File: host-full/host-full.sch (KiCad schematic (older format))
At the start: 17 parts, among them J1 CONN_INTEGRALSTICK_MCU_HOST, J15 XILINX_JTAG, J16 Conn_Coaxial, J17 Conn_Coaxial, J18 Conn_Coaxial, J19 Conn_Coaxial, J2 CONN_INTEGRALSTICK_FPGA_HOST, J20 Conn_Coaxial, J21 Conn_Coaxial, SW1 SW_SPST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

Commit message: Finished initial schematic review
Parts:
- added J23: PMOD_HOST, symbol special-azonenberg:PMOD_HOST
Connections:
- net 3V3: now also J23.12 (3V3), J23.6 (3V3)
- net GND: now also J23.11 (GND), J23.5 (GND)
- net LVDS_DQ5_N: now reaches J2.21 (LVDS_DQ5_N)
- net LVDS_DQ5_N: now also J23.10 (D7)
- net LVDS_DQ4_N: now reaches J2.22 (LVDS_DQ4_N)
- net LVDS_DQ4_N: now also J23.8 (D5)
- net LVDS_DQ5_P: now reaches J2.23 (LVDS_DQ5_P)
- net LVDS_DQ5_P: now also J23.9 (D6)
- net LVDS_DQ4_P: now reaches J2.24 (LVDS_DQ4_P)
- net LVDS_DQ4_P: now also J23.7 (D4)
- net LVDS_DQ3_N: now reaches J2.27 (LVDS_DQ3_N)
- net LVDS_DQ3_N: now also J23.4 (D3)
- net LVDS_DQ2_N: now reaches J2.28 (LVDS_DQ2_N)
- net LVDS_DQ2_N: now also J23.2 (D1)
- net LVDS_DQ3_P: now reaches J2.29 (LVDS_DQ3_P)
- net LVDS_DQ3_P: now also J23.3 (D2)
- net LVDS_DQ2_P: now reaches J2.30 (LVDS_DQ2_P)
- net LVDS_DQ2_P: now also J23.1 (D0)
- no-connect marks 16 -> 8
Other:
- note removed: "Ethernet 2V5, 1V2 are high power rails we need to generate\n1V8, 3V3 are just RGMII power"
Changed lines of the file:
@@
 Sheet 1 4
 Title "INTEGRALSTICK Full Host"
-Date "2019-11-03"
+Date "2019-11-04"
 Rev "0.1"
 Comp "Antikernel Labs"
@@
 Comment4 ""
 $EndDescr
-$Comp
-L special-azonenberg:CONN_INTEGRALSTICK_FPGA_HOST J2
-U 3 1 5DBBCD32
-P 9600 5900
-F 0 "J2" H 9600 5850 50  0000 L CNN
-F 1 "CONN_INTEGRALSTICK_FPGA_HOST" H 9600 5750 50  0000 L CNN
-F 2 "" H 9600 5900 50  0001 C CNN
-F 3 "" H 9600 5900 50  0001 C CNN
-	3    9600 5900
-	1    0    0    -1
-$EndComp
 $Sheet
 S 700  850  800  650
@@
 F1 "psu.sch" 50
 F2 "GND" O R 1500 1400 50
-F4 "3V3" O R 1500 1000 50
-F5 "1V8" O R 1500 1200 50
+F3 "3V3" O R 1500 1000 50
+F4 "1V8" O R 1500 1200 50
+F5 "2V5" O R 1500 1100 50
+F6 "1V2" O R 1500 1300 50
 $EndSheet
 $Sheet
@@
 Text Label 1800 5750 0    50   ~ 0
 3V3
-Text Notes 700  700  0    50   ~ 0
-Ethernet 2V5, 1V2 are high power rails we need to generate\n1V8, 3V3 are just RGMII power
 Text Label 1500 2450 0    50   ~ 0
-ETH_2V5
+2V5
 Text Label 1500 2350 0    50   ~ 0
 3V3
@@
 1V8
 Text Label 1500 2650 0    50   ~ 0
-ETH_1V2
+1V2
 Text Label 1800 5850 0    50   ~ 0
 GND
@@
 Text Label 9400 3450 2    50   ~ 0
 LVDS_DQ1_N
-NoConn ~ 9400 3650
-NoConn ~ 9400 3750
-NoConn ~ 9400 3950
-NoConn ~ 9400 4050
-NoConn ~ 9400 4250
-NoConn ~ 9400 4350
-NoConn ~ 9400 4550
-NoConn ~ 9400 4650
 NoConn ~ 9400 4850
 NoConn ~ 9400 4950
@@
 Text Label 9400 5850 2    50   ~ 0
 ETH0_LED2_P
+Text Label 1500 1100 0    50   ~ 0
+2V5
+Text Label 1500 1300 0    50   ~ 0
+1V2
+Wire Wire Line
+	7000 3200 7000 3300
+Wire Wire Line
+	7000 3400 7000 3500
+Text Label 7000 3700 0    50   ~ 0
+LVDS_DQ2_P
+Text Label 7000 3800 0    50   ~ 0
+LVDS_DQ2_N
+Text Label 7000 3900 0    50   ~ 0
+LVDS_DQ3_P
+Text Label 7000 4000 0    50   ~ 0
+LVDS_DQ3_N
+Text Label 7000 4100 0    50   ~ 0
+LVDS_DQ4_P
+Text Label 7000 4200 0    50   ~ 0
+LVDS_DQ4_N
+$Comp
+L special-azonenberg:PMOD_HOST J?
+U 1 1 5E1F1FA5
+P 6800 4450
+AR Path="/5DF8FFFE/5E1F1FA5" Ref="J?"  Part="1"
+AR Path="/5E1F1FA5" Ref="J23"  Part="1"
+F 0 "J23" H 6867 5947 60  0000 C CNN
+F 1 "PMOD_HOST" H 6867 5841 60  0000 C CNN
+F 2 "" H 6800 4450 60  0001 C CNN
+F 3 "" H 6800 4450 60  0001 C CNN
+	1    6800 4450
+	-1   0    0    -1
+$EndComp
+Text Label 7000 4300 0    50   ~ 0
+LVDS_DQ5_P
+Text Label 7000 4400 0    50   ~ 0
+LVDS_DQ5_N
+$Comp
+L special-azonenberg:CONN_INTEGRALSTICK_FPGA_HOST J2
+U 3 1 5DBBCD32
+P 9600 5900
+F 0 "J2" H 9600 5850 50  0000 L CNN
+F 1 "CONN_INTEGRALSTICK_FPGA_HOST" H 9600 5750 50  0000 L CNN
+F 2 "" H 9600 5900 50  0001 C CNN
+F 3 "" H 9600 5900 50  0001 C CNN
+	3    9600 5900
+	1    0    0    -1
+$EndComp
+Text Label 9400 3650 2    50   ~ 0
+LVDS_DQ2_P
+Text Label 9400 3750 2    50   ~ 0
+LVDS_DQ2_N
+Text Label 9400 3950 2    50   ~ 0
+LVDS_DQ3_P
+Text Label 9400 4050 2    50   ~ 0
+LVDS_DQ3_N
+Text Label 9400 4250 2    50   ~ 0
+LVDS_DQ4_P
+Text Label 9400 4350 2    50   ~ 0
+LVDS_DQ4_N
+Text Label 9400 4550 2    50   ~ 0
+LVDS_DQ5_P
+Text Label 9400 4650 2    50   ~ 0
+LVDS_DQ5_N
+Text Label 7000 3200 0    50   ~ 0
+3V3
+Text Label 7000 3400 0    50   ~ 0
+GND
 $EndSCHEMATC

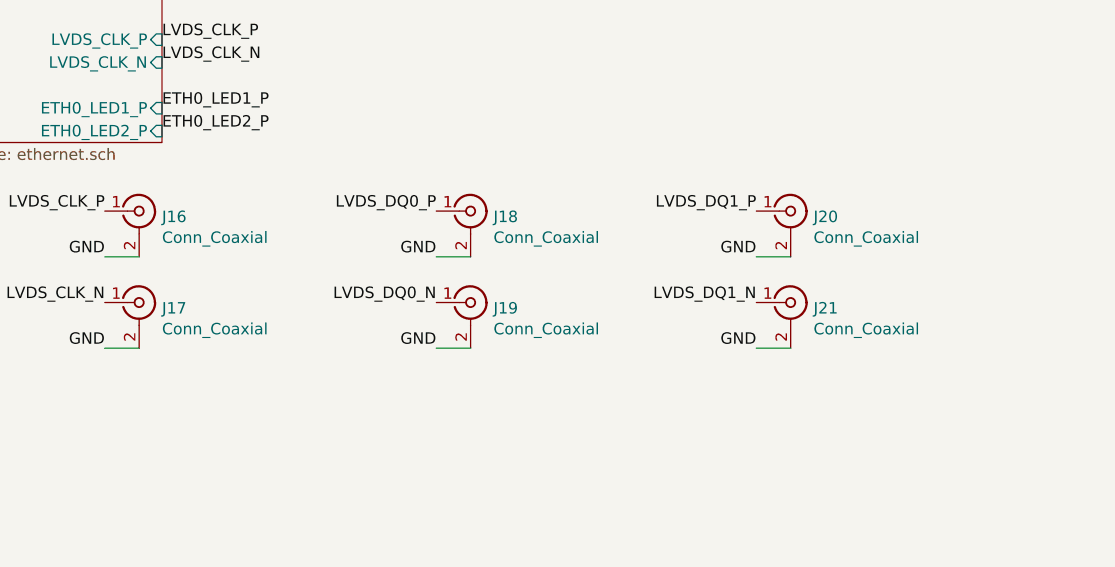
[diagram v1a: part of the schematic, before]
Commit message: Initial layout on host-full. Rough floorplan is finalized, all MCU PMODs routed.
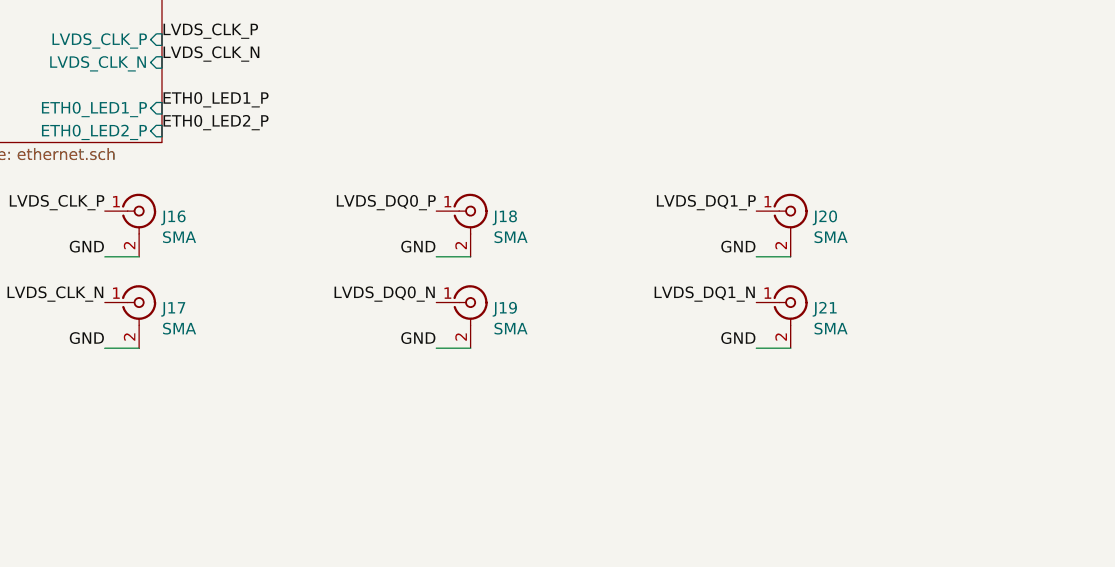
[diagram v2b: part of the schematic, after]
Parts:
- D1: footprint (none) -> azonenberg_pcb:EIA_0603_LED
- J1, J2: footprint (none) -> azonenberg_pcb:CONN_SAMTEC_QSH-060-01-L-D-A
- J15: footprint (none) -> azonenberg_pcb:XILINX_JTAG_PTH_MOLEX_0878311420
- J16, J17, J18, J19, J20, J21: value Conn_Coaxial -> SMA; footprint (none) -> azonenberg_pcb:CONN_SMA_EDGE_SAMTEC_SMA_J_P_H_ST_EM1
- J23: footprint (none) -> azonenberg_pcb:CONN_HEADER_2.54MM_2x6_RA_PMOD_HOST
- R49, R50, R51, R52: footprint (none) -> azonenberg_pcb:EIA_0402_RES_NOSILK
- SW1, SW2, SW3: footprint (none) -> azonenberg_pcb:SWITCH_RAFI_MICON_5
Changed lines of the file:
@@
 Sheet 1 4
 Title "INTEGRALSTICK Full Host"
-Date "2019-11-04"
+Date "2019-11-07"
 Rev "0.1"
 Comp "Antikernel Labs"
@@
 F 0 "J1" H 3578 6901 50  0000 L CNN
 F 1 "CONN_INTEGRALSTICK_MCU_HOST" H 3578 6810 50  0000 L CNN
-F 2 "" H 3000 6400 50  0001 C CNN
+F 2 "azonenberg_pcb:CONN_SAMTEC_QSH-060-01-L-D-A" H 3000 6400 50  0001 C CNN
 F 3 "" H 3000 6400 50  0001 C CNN
 	2    3000 6400
@@
 F 0 "SW1" V 3004 6998 50  0000 L CNN
 F 1 "SW_SPST" V 3095 6998 50  0000 L CNN
-F 2 "" H 3050 6900 50  0001 C CNN
+F 2 "azonenberg_pcb:SWITCH_RAFI_MICON_5" H 3050 6900 50  0001 C CNN
 F 3 "" H 3050 6900 50  0001 C CNN
 	1    3050 6900
@@
 F 0 "J15" H 2138 8397 60  0000 C CNN
 F 1 "XILINX_JTAG" H 2138 8291 60  0000 C CNN
-F 2 "" H 1800 6850 60  0000 C CNN
+F 2 "azonenberg_pcb:XILINX_JTAG_PTH_MOLEX_0878311420" H 1800 6850 60  0001 C CNN
 F 3 "" H 1800 6850 60  0000 C CNN
 	1    1800 6850
@@
 F 0 "R49" H 3120 7296 50  0000 L CNN
 F 1 "DNP" H 3120 7205 50  0000 L CNN
-F 2 "" V 2980 7250 50  0001 C CNN
+F 2 "azonenberg_pcb:EIA_0402_RES_NOSILK" V 2980 7250 50  0001 C CNN
 F 3 "" H 3050 7250 50  0001 C CNN
 	1    3050 7250
@@
 F 0 "R50" H 4020 6996 50  0000 L CNN
 F 1 "DNP" H 4020 6905 50  0000 L CNN
-F 2 "" V 3880 6950 50  0001 C CNN
+F 2 "azonenberg_pcb:EIA_0402_RES_NOSILK" V 3880 6950 50  0001 C CNN
 F 3 "" H 3950 6950 50  0001 C CNN
 	1    3950 6950
@@
 F 0 "SW2" V 3904 7398 50  0000 L CNN
 F 1 "SW_SPST" V 3995 7398 50  0000 L CNN
-F 2 "" H 3950 7300 50  0001 C CNN
+F 2 "azonenberg_pcb:SWITCH_RAFI_MICON_5" H 3950 7300 50  0001 C CNN
 F 3 "" H 3950 7300 50  0001 C CNN
 	1    3950 7300
@@
 F 0 "R51" H 4920 6996 50  0000 L CNN
 F 1 "DNP" H 4920 6905 50  0000 L CNN
-F 2 "" V 4780 6950 50  0001 C CNN
+F 2 "azonenberg_pcb:EIA_0402_RES_NOSILK" V 4780 6950 50  0001 C CNN
 F 3 "" H 4850 6950 50  0001 C CNN
 	1    4850 6950
@@
 F 0 "SW3" V 4804 7398 50  0000 L CNN
 F 1 "SW_SPST" V 4895 7398 50  0000 L CNN
-F 2 "" H 4850 7300 50  0001 C CNN
+F 2 "azonenberg_pcb:SWITCH_RAFI_MICON_5" H 4850 7300 50  0001 C CNN
 F 3 "" H 4850 7300 50  0001 C CNN
 	1    4850 7300
@@
 F 0 "R52" H 5770 6996 50  0000 L CNN
 F 1 "270" H 5770 6905 50  0000 L CNN
-F 2 "" V 5630 6950 50  0001 C CNN
+F 2 "azonenberg_pcb:EIA_0402_RES_NOSILK" V 5630 6950 50  0001 C CNN
 F 3 "" H 5700 6950 50  0001 C CNN
 	1    5700 6950
@@
 F 0 "D1" V 5739 7132 50  0000 R CNN
 F 1 "GREEN" V 5648 7132 50  0000 R CNN
-F 2 "" H 5700 7250 50  0001 C CNN
+F 2 "azonenberg_pcb:EIA_0603_LED" H 5700 7250 50  0001 C CNN
 F 3 "~" H 5700 7250 50  0001 C CNN
 	1    5700 7250
@@
 P 1400 3700
 F 0 "J16" H 1500 3675 50  0000 L CNN
-F 1 "Conn_Coaxial" H 1500 3584 50  0000 L CNN
-F 2 "" H 1400 3700 50  0001 C CNN
+F 1 "SMA" H 1500 3584 50  0000 L CNN
+F 2 "azonenberg_pcb:CONN_SMA_EDGE_SAMTEC_SMA_J_P_H_ST_EM1" H 1400 3700 50  0001 C CNN
 F 3 "" H 1400 3700 50  0001 C CNN
 	1    1400 3700
@@
 P 1400 4100
 F 0 "J17" H 1500 4075 50  0000 L CNN
-F 1 "Conn_Coaxial" H 1500 3984 50  0000 L CNN
-F 2 "" H 1400 4100 50  0001 C CNN
+F 1 "SMA" H 1500 3984 50  0000 L CNN
+F 2 "azonenberg_pcb:CONN_SMA_EDGE_SAMTEC_SMA_J_P_H_ST_EM1" H 1400 4100 50  0001 C CNN
 F 3 "" H 1400 4100 50  0001 C CNN
 	1    1400 4100
@@
 P 2850 3700
 F 0 "J18" H 2950 3675 50  0000 L CNN
-F 1 "Conn_Coaxial" H 2950 3584 50  0000 L CNN
-F 2 "" H 2850 3700 50  0001 C CNN
+F 1 "SMA" H 2950 3584 50  0000 L CNN
+F 2 "azonenberg_pcb:CONN_SMA_EDGE_SAMTEC_SMA_J_P_H_ST_EM1" H 2850 3700 50  0001 C CNN
 F 3 "" H 2850 3700 50  0001 C CNN
 	1    2850 3700
@@
 P 2850 4100
 F 0 "J19" H 2950 4075 50  0000 L CNN
-F 1 "Conn_Coaxial" H 2950 3984 50  0000 L CNN
-F 2 "" H 2850 4100 50  0001 C CNN
+F 1 "SMA" H 2950 3984 50  0000 L CNN
+F 2 "azonenberg_pcb:CONN_SMA_EDGE_SAMTEC_SMA_J_P_H_ST_EM1" H 2850 4100 50  0001 C CNN
 F 3 "" H 2850 4100 50  0001 C CNN
 	1    2850 4100
@@
 P 4250 3700
 F 0 "J20" H 4350 3675 50  0000 L CNN
-F 1 "Conn_Coaxial" H 4350 3584 50  0000 L CNN
-F 2 "" H 4250 3700 50  0001 C CNN
+F 1 "SMA" H 4350 3584 50  0000 L CNN
+F 2 "azonenberg_pcb:CONN_SMA_EDGE_SAMTEC_SMA_J_P_H_ST_EM1" H 4250 3700 50  0001 C CNN
 F 3 "" H 4250 3700 50  0001 C CNN
 	1    4250 3700
@@
 P 4250 4100
 F 0 "J21" H 4350 4075 50  0000 L CNN
-F 1 "Conn_Coaxial" H 4350 3984 50  0000 L CNN
-F 2 "" H 4250 4100 50  0001 C CNN
+F 1 "SMA" H 4350 3984 50  0000 L CNN
+F 2 "azonenberg_pcb:CONN_SMA_EDGE_SAMTEC_SMA_J_P_H_ST_EM1" H 4250 4100 50  0001 C CNN
 F 3 "" H 4250 4100 50  0001 C CNN
 	1    4250 4100
@@
 F 0 "J23" H 6867 5947 60  0000 C CNN
 F 1 "PMOD_HOST" H 6867 5841 60  0000 C CNN
-F 2 "" H 6800 4450 60  0001 C CNN
+F 2 "azonenberg_pcb:CONN_HEADER_2.54MM_2x6_RA_PMOD_HOST" H 6800 4450 60  0001 C CNN
 F 3 "" H 6800 4450 60  0001 C CNN
 	1    6800 4450
@@
 F 0 "J2" H 9600 5850 50  0000 L CNN
 F 1 "CONN_INTEGRALSTICK_FPGA_HOST" H 9600 5750 50  0000 L CNN
-F 2 "" H 9600 5900 50  0001 C CNN
+F 2 "azonenberg_pcb:CONN_SAMTEC_QSH-060-01-L-D-A" H 9600 5900 50  0001 C CNN
 F 3 "" H 9600 5900 50  0001 C CNN
 	3    9600 5900

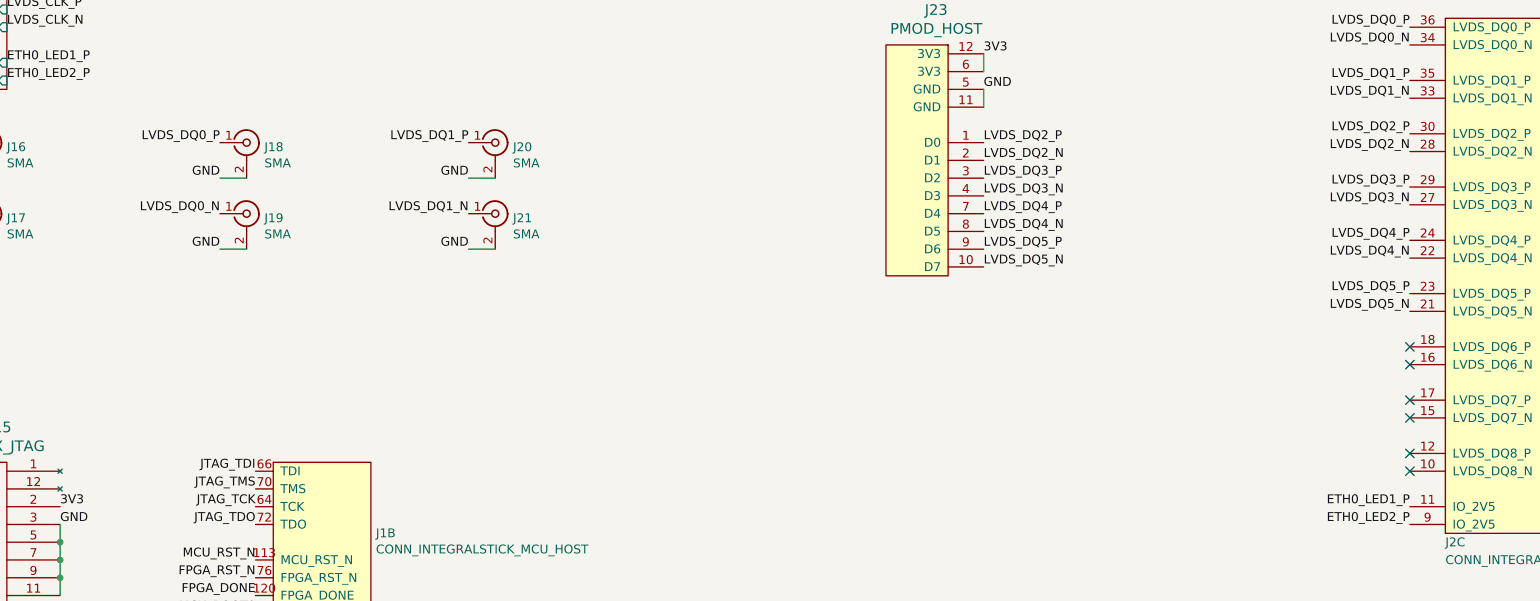
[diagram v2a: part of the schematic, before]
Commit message: Continued host-full layout. Almost all PHY RGMII routing done
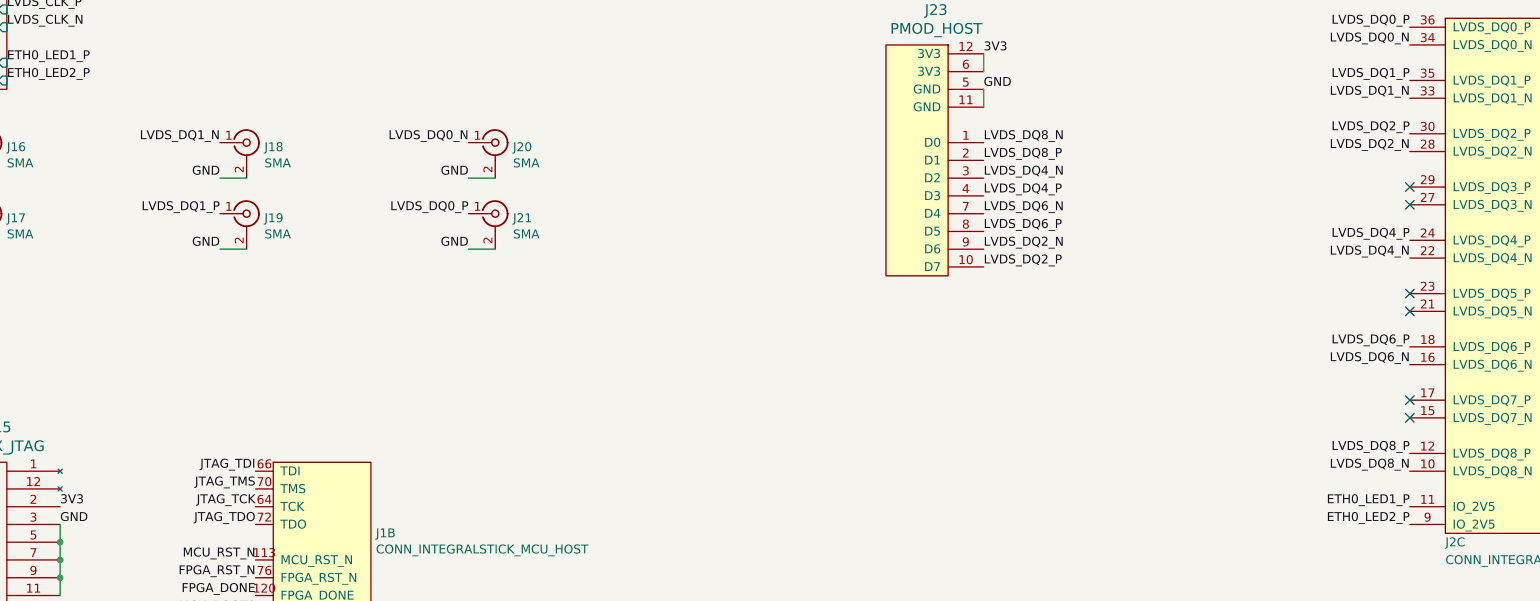
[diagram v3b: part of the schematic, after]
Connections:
- net LVDS_DQ0_N: now also J20.1 (In); no longer J19.1 (In)
- net LVDS_DQ0_P: now also J21.1 (In); no longer J18.1 (In)
- net LVDS_DQ1_N: now also J18.1 (In); no longer J21.1 (In)
- net LVDS_DQ1_P: now also J19.1 (In); no longer J20.1 (In)
- net LVDS_DQ2_N: now also J23.9 (D6); no longer J23.2 (D1)
- net LVDS_DQ2_P: now also J23.10 (D7); no longer J23.1 (D0)
- net LVDS_DQ4_N: now also J23.3 (D2); no longer J23.8 (D5)
- net LVDS_DQ4_P: now also J23.4 (D3); no longer J23.7 (D4)
- net LVDS_DQ8_N: now reaches J2.10 (LVDS_DQ8_N)
- net LVDS_DQ8_N: now also J23.1 (D0)
- net LVDS_DQ8_P: now reaches J2.12 (LVDS_DQ8_P)
- net LVDS_DQ8_P: now also J23.2 (D1)
- net LVDS_DQ6_N: now reaches J2.16 (LVDS_DQ6_N)
- net LVDS_DQ6_N: now also J23.7 (D4)
- net LVDS_DQ6_P: now reaches J2.18 (LVDS_DQ6_P)
- net LVDS_DQ6_P: now also J23.8 (D5)
- net LVDS_DQ3_N: no longer names the net of J2.27 (LVDS_DQ3_N)
- net LVDS_DQ3_N: no longer J23.4 (D3)
- net LVDS_DQ3_P: no longer names the net of J2.29 (LVDS_DQ3_P)
- net LVDS_DQ3_P: no longer J23.3 (D2)
- net LVDS_DQ5_N: no longer names the net of J2.21 (LVDS_DQ5_N)
- net LVDS_DQ5_N: no longer J23.10 (D7)
- net LVDS_DQ5_P: no longer names the net of J2.23 (LVDS_DQ5_P)
- net LVDS_DQ5_P: no longer J23.9 (D6)
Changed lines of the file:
@@
 Sheet 1 4
 Title "INTEGRALSTICK Full Host"
-Date "2019-11-07"
+Date "2019-11-08"
 Rev "0.1"
 Comp "Antikernel Labs"
@@
 	1    0    0    -1
 $EndComp
-Text Label 2700 3700 2    50   ~ 0
+Text Label 4100 4100 2    50   ~ 0
 LVDS_DQ0_P
 Text Label 2700 3900 2    50   ~ 0
@@
 	1    0    0    -1
 $EndComp
-Text Label 2700 4100 2    50   ~ 0
+Text Label 4100 3700 2    50   ~ 0
 LVDS_DQ0_N
 Text Label 2700 4300 2    50   ~ 0
@@
 	1    0    0    -1
 $EndComp
-Text Label 4100 3700 2    50   ~ 0
+Text Label 2700 4100 2    50   ~ 0
 LVDS_DQ1_P
 Text Label 4100 3900 2    50   ~ 0
@@
 	1    0    0    -1
 $EndComp
-Text Label 4100 4100 2    50   ~ 0
+Text Label 2700 3700 2    50   ~ 0
 LVDS_DQ1_N
 Text Label 4100 4300 2    50   ~ 0
@@
 Text Label 9400 3450 2    50   ~ 0
 LVDS_DQ1_N
-NoConn ~ 9400 4850
-NoConn ~ 9400 4950
 NoConn ~ 9400 5150
 NoConn ~ 9400 5250
-NoConn ~ 9400 5450
-NoConn ~ 9400 5550
 Text Label 1500 1000 0    50   ~ 0
 3V3
@@
 Wire Wire Line
 	7000 3400 7000 3500
-Text Label 7000 3700 0    50   ~ 0
+Text Label 7000 4400 0    50   ~ 0
 LVDS_DQ2_P
-Text Label 7000 3800 0    50   ~ 0
+Text Label 7000 4300 0    50   ~ 0
 LVDS_DQ2_N
+Text Label 7000 4200 0    50   ~ 0
+LVDS_DQ6_P
+Text Label 7000 4100 0    50   ~ 0
+LVDS_DQ6_N
+Text Label 7000 4000 0    50   ~ 0
+LVDS_DQ4_P
 Text Label 7000 3900 0    50   ~ 0
-LVDS_DQ3_P
-Text Label 7000 4000 0    50   ~ 0
-LVDS_DQ3_N
-Text Label 7000 4100 0    50   ~ 0
-LVDS_DQ4_P
-Text Label 7000 4200 0    50   ~ 0
 LVDS_DQ4_N
 $Comp
@@
 	-1   0    0    -1
 $EndComp
-Text Label 7000 4300 0    50   ~ 0
-LVDS_DQ5_P
-Text Label 7000 4400 0    50   ~ 0
-LVDS_DQ5_N
+Text Label 7000 3800 0    50   ~ 0
+LVDS_DQ8_P
+Text Label 7000 3700 0    50   ~ 0
+LVDS_DQ8_N
 $Comp
 L special-azonenberg:CONN_INTEGRALSTICK_FPGA_HOST J2
@@
 Text Label 9400 3750 2    50   ~ 0
 LVDS_DQ2_N
-Text Label 9400 3950 2    50   ~ 0
-LVDS_DQ3_P
-Text Label 9400 4050 2    50   ~ 0
-LVDS_DQ3_N
+Text Label 9400 4850 2    50   ~ 0
+LVDS_DQ6_P
+Text Label 9400 4950 2    50   ~ 0
+LVDS_DQ6_N
 Text Label 9400 4250 2    50   ~ 0
 LVDS_DQ4_P
 Text Label 9400 4350 2    50   ~ 0
 LVDS_DQ4_N
-Text Label 9400 4550 2    50   ~ 0
-LVDS_DQ5_P
-Text Label 9400 4650 2    50   ~ 0
-LVDS_DQ5_N
+Text Label 9400 5450 2    50   ~ 0
+LVDS_DQ8_P
+Text Label 9400 5550 2    50   ~ 0
+LVDS_DQ8_N
 Text Label 7000 3200 0    50   ~ 0
 3V3
 Text Label 7000 3400 0    50   ~ 0
 GND
+NoConn ~ 9400 4650
+NoConn ~ 9400 4550
+NoConn ~ 9400 4050
+NoConn ~ 9400 3950
 $EndSCHEMATC

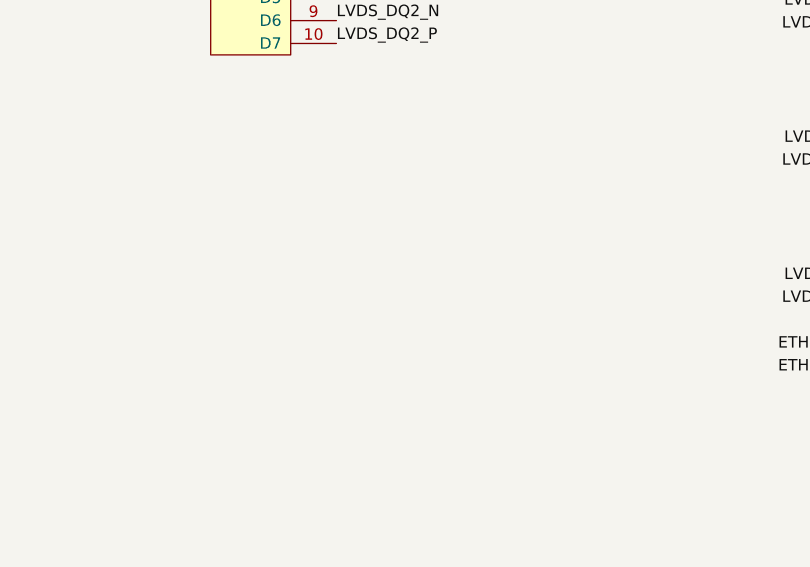
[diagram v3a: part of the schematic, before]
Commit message: Various fixes during layout review, added some silkscreen labels and a layer-change cap
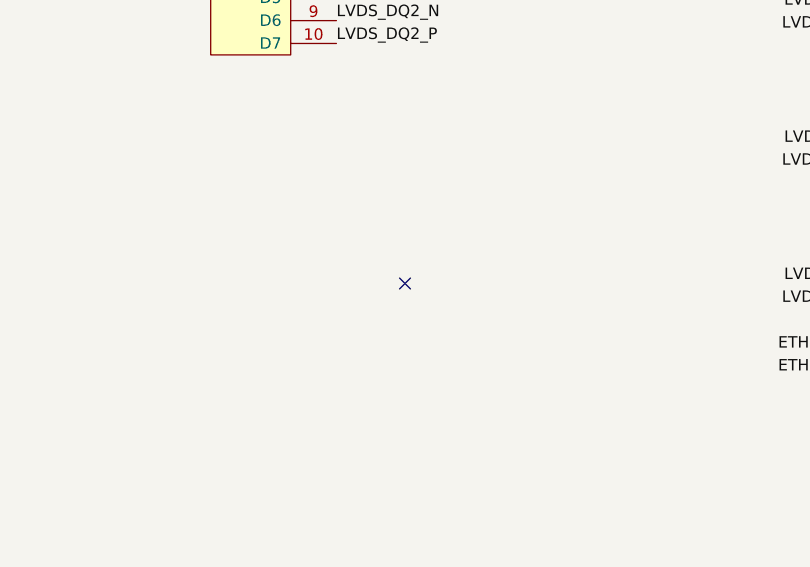
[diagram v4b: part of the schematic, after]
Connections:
- no-connect marks 8 -> 9
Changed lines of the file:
@@
 Sheet 1 4
 Title "INTEGRALSTICK Full Host"
-Date "2019-11-08"
+Date "2019-11-10"
 Rev "0.1"
 Comp "Antikernel Labs"
@@
 NoConn ~ 9400 4050
 NoConn ~ 9400 3950
+NoConn ~ 7300 5450
 $EndSCHEMATC
